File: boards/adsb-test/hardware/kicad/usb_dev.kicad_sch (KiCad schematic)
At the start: 0 parts

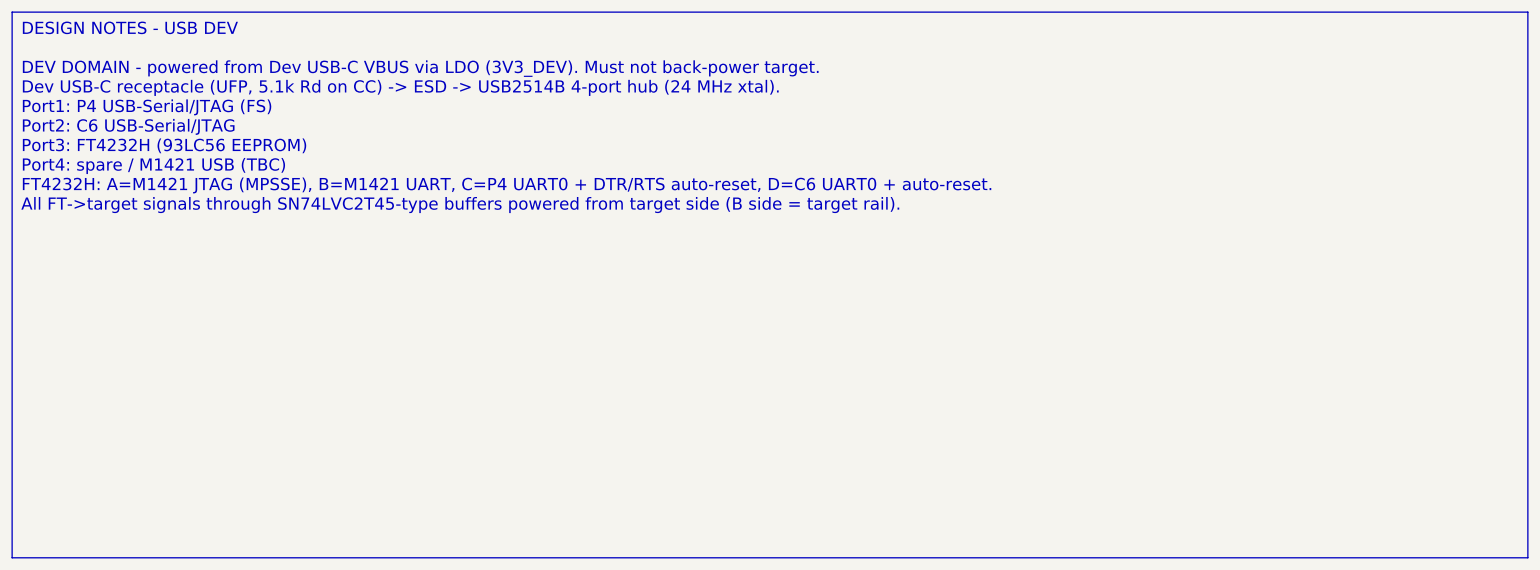
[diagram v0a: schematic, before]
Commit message: Release v0.4.0: ADSB_Test with ESP32-C5, ADSBee m1421 and LA5016 header
- C6 -> C5 co-processor; m1421 identified and integrated (symbol/footprint
  from the ADSBee 1421 carrier, GPL-3.0 attribution)
- Power budget and 2S1P battery sizing for >= 1 h; USB-A for 1-2 SDRs via hub
- Dev port: FT2232H + RP2040 debugprobe; TCA6408A expander for slow I/O
- Test Debug sheet with LA5016 header and rail test points
- Vendor documents git-ignored (public repo)

Co-Authored-By: Claude Opus 5.5 <noreply@anthropic.com>
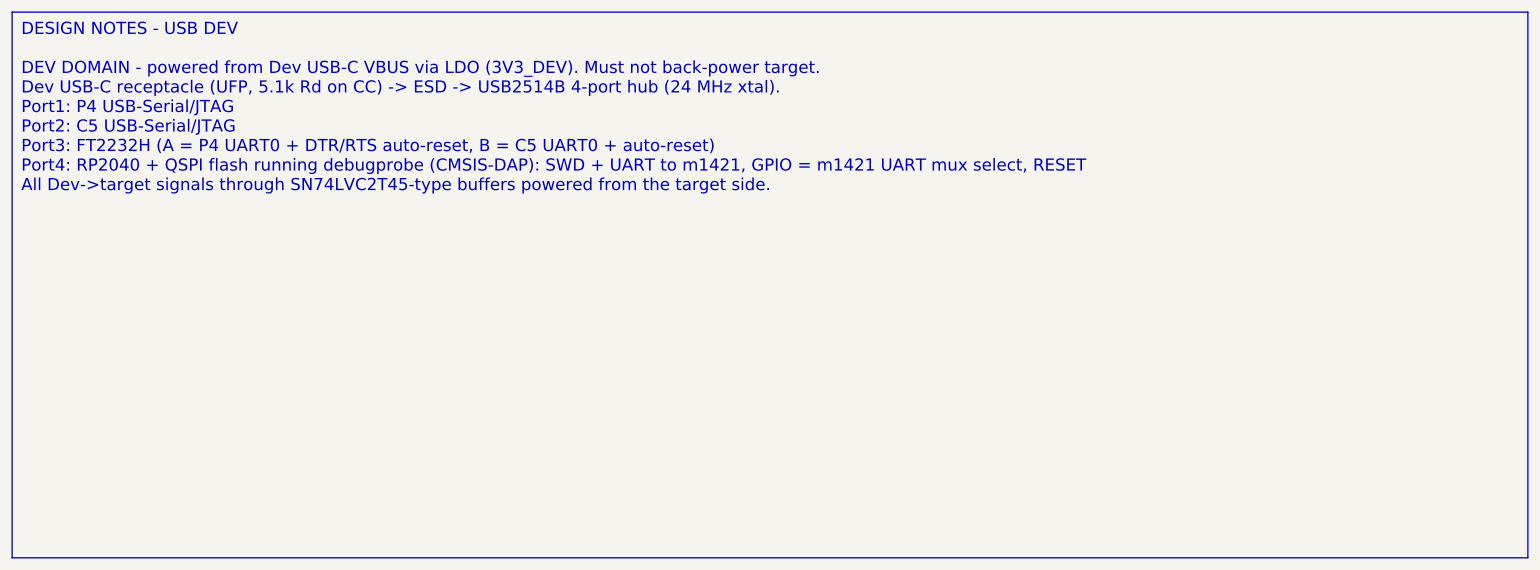
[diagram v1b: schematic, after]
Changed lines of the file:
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@@
 		(comment 1 "Requirements: boards/adsb-test/docs/requirements.md")
 	)
-	(text_box "DESIGN NOTES - USB DEV\n\nDEV DOMAIN - powered from Dev USB-C VBUS via LDO (3V3_DEV). Must not back-power target.\nDev USB-C receptacle (UFP, 5.1k Rd on CC) -> ESD -> USB2514B 4-port hub (24 MHz xtal).\n  Port1: P4 USB-Serial/JTAG (FS)\n  Port2: C6 USB-Serial/JTAG\n  Port3: FT4232H (93LC56 EEPROM)\n  Port4: spare / M1421 USB (TBC)\nFT4232H: A=M1421 JTAG (MPSSE), B=M1421 UART, C=P4 UART0 + DTR/RTS auto-reset, D=C6 UART0 + auto-reset.\nAll FT->target signals through SN74LVC2T45-type buffers powered from target side (B side = target rail)."
+	(text_box "DESIGN NOTES - USB DEV\n\nDEV DOMAIN - powered from Dev USB-C VBUS via LDO (3V3_DEV). Must not back-power target.\nDev USB-C receptacle (UFP, 5.1k Rd on CC) -> ESD -> USB2514B 4-port hub (24 MHz xtal).\n  Port1: P4 USB-Serial/JTAG\n  Port2: C5 USB-Serial/JTAG\n  Port3: FT2232H (A = P4 UART0 + DTR/RTS auto-reset, B = C5 UART0 + auto-reset)\n  Port4: RP2040 + QSPI flash running debugprobe (CMSIS-DAP): SWD + UART to m1421, GPIO = m1421 UART mux select, RESET\nAll Dev->target signals through SN74LVC2T45-type buffers powered from the target side."
 		(exclude_from_sim no)
 		(at 20 20 0)
